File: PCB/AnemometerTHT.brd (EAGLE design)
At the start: 150 x 100 mm, 36 parts, among them IC1 TINY2313A, IC2 74HC151D, IC3 74HC151D, IC4 74HC08D, IC5 LM555N, IC6 74HC138D, IC7 74CH14D, IC8 74HC393D, Q1 16MHz

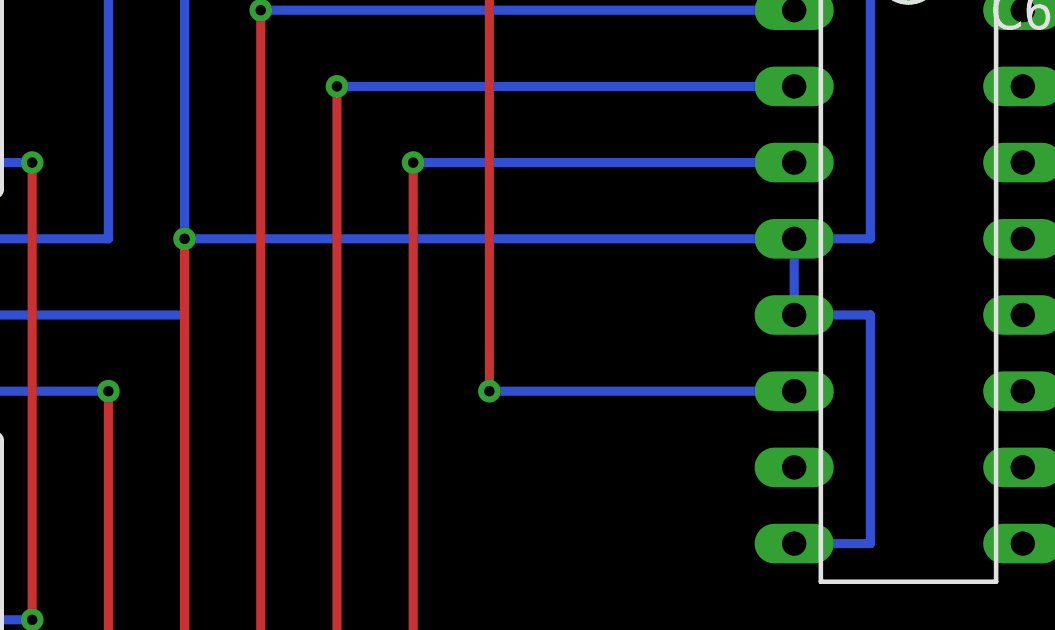
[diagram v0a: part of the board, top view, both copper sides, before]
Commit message: realized that i inverted the wrong signal
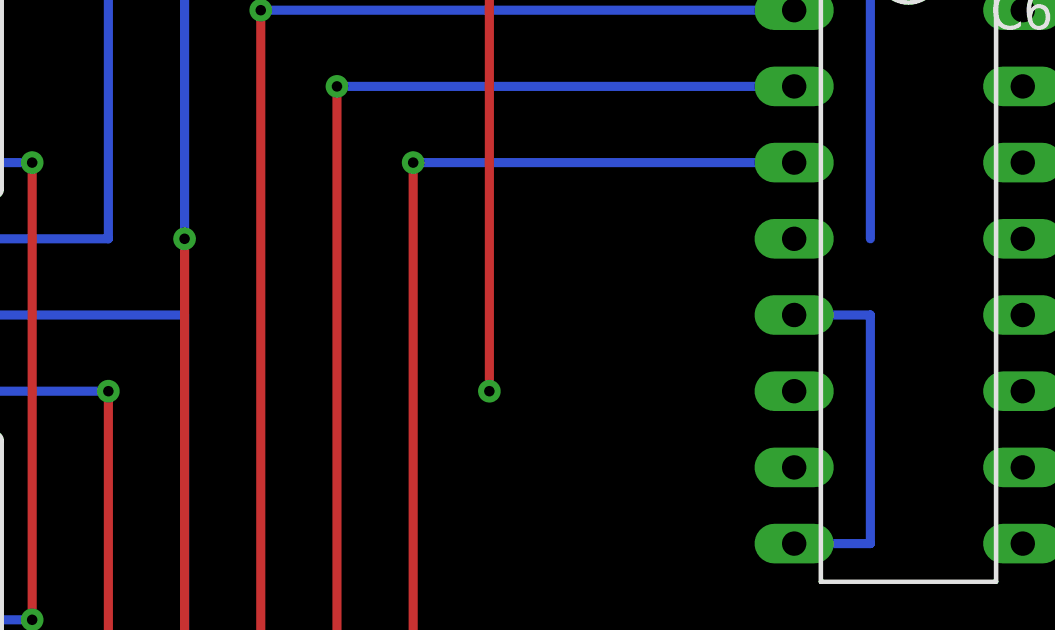
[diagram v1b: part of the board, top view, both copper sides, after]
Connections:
- net GND: no longer IC6.4
- net TRIG: now also IC6.4; no longer IC6.6
- net VCC: now also IC6.6
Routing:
- net GND: track 660.4 -> 635.0 mm
- net TRIG: track 127.0 -> 116.8 mm
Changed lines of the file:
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@@
 <contactref element="IC1" pad="7"/>
 <contactref element="IC8" pad="2"/>
-<contactref element="IC6" pad="6"/>
 <wire x1="30.48" y1="55.88" x2="38.1" y2="55.88" width="0.3048" layer="16"/>
 <wire x1="38.1" y1="55.88" x2="38.1" y2="86.36" width="0.3048" layer="16"/>
@@
 <wire x1="38.1" y1="96.52" x2="58.42" y2="96.52" width="0.3048" layer="16"/>
 <wire x1="58.42" y1="96.52" x2="58.42" y2="91.44" width="0.3048" layer="16"/>
-<wire x1="91.44" y1="76.2" x2="81.28" y2="76.2" width="0.3048" layer="16"/>
 <via x="81.28" y="76.2" extent="1-16" drill="0.35"/>
 <wire x1="81.28" y1="96.52" x2="81.28" y2="76.2" width="0.3048" layer="1"/>
 <via x="81.28" y="96.52" extent="1-16" drill="0.35"/>
 <wire x1="81.28" y1="96.52" x2="58.42" y2="96.52" width="0.3048" layer="16"/>
+<contactref element="IC6" pad="4"/>
+<wire x1="81.28" y1="76.2" x2="91.44" y2="81.28" width="0" layer="19" extent="1-1"/>
 </signal>
 <signal name="UART_TX">
@@
 <contactref element="IC2" pad="12"/>
 <contactref element="IC6" pad="5"/>
-<contactref element="IC6" pad="4"/>
 <contactref element="R8" pad="1"/>
 <contactref element="R3" pad="1"/>
@@
 <via x="132.08" y="81.28" extent="1-16" drill="0.35"/>
 <wire x1="132.08" y1="81.28" x2="132.08" y2="66.04" width="0.3048" layer="1"/>
-<wire x1="91.44" y1="81.28" x2="91.44" y2="78.74" width="0.3048" layer="16"/>
 <wire x1="91.44" y1="71.12" x2="93.98" y2="71.12" width="0.3048" layer="16"/>
 <wire x1="93.98" y1="71.12" x2="93.98" y2="78.74" width="0.3048" layer="16"/>
@@
 <wire x1="83.82" y1="22.86" x2="91.44" y2="22.86" width="0.3048" layer="16"/>
 <wire x1="101.6" y1="22.86" x2="134.62" y2="22.86" width="0.3048" layer="16"/>
-<wire x1="91.44" y1="81.28" x2="71.12" y2="81.28" width="0.3048" layer="16"/>
 <wire x1="134.62" y1="7.62" x2="132.08" y2="7.62" width="0.3048" layer="16"/>
 <via x="132.08" y="7.62" extent="1-16" drill="0.35"/>
@@
 <via x="48.26" y="66.04" extent="1-16" drill="0.35"/>
 <wire x1="48.26" y1="66.04" x2="48.26" y2="68.58" width="0.3048" layer="16"/>
-<wire x1="91.44" y1="81.28" x2="93.98" y2="81.28" width="0.3048" layer="16"/>
 <wire x1="48.26" y1="68.58" x2="48.26" y2="73.66" width="0.3048" layer="16"/>
 <wire x1="48.26" y1="73.66" x2="45.72" y2="73.66" width="0.3048" layer="16"/>
@@
 <wire x1="63.5" y1="45.72" x2="63.5" y2="55.88" width="0.3048" layer="16"/>
 <via x="71.12" y="55.88" extent="1-16" drill="0.35"/>
+<wire x1="91.44" y1="78.74" x2="93.98" y2="81.28" width="0" layer="19" extent="16-16"/>
+<wire x1="83.82" y1="55.88" x2="91.44" y2="71.12" width="0" layer="19" extent="1-1"/>
 </signal>
 <signal name="VCC">
@@
 <wire x1="71.12" y1="43.18" x2="60.96" y2="43.18" width="0.3048" layer="16"/>
 <wire x1="86.36" y1="10.16" x2="58.42" y2="10.16" width="0.3048" layer="16"/>
+<contactref element="IC6" pad="6"/>
+<wire x1="99.06" y1="88.9" x2="91.44" y2="76.2" width="0" layer="19" extent="1-1"/>
 </signal>
 <signal name="PULS">

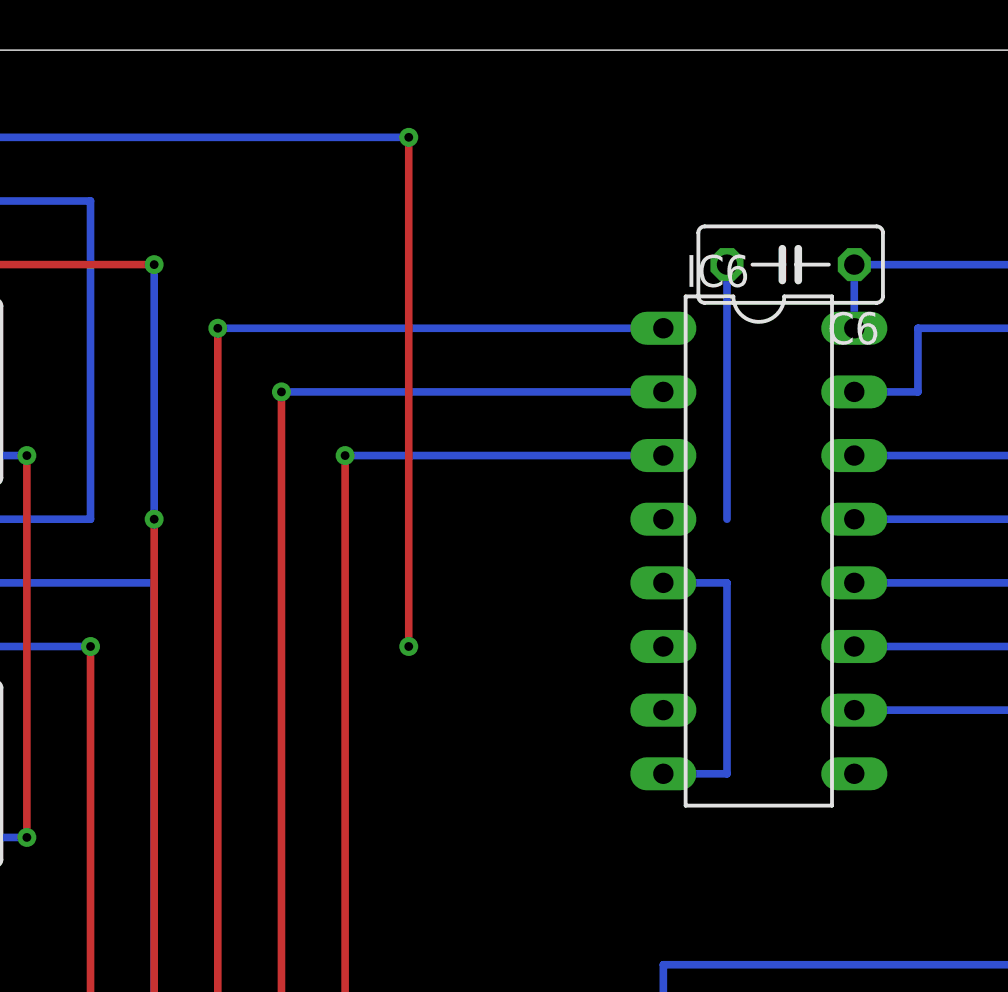
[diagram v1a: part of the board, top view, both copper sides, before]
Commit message: corrected multilexer addressing
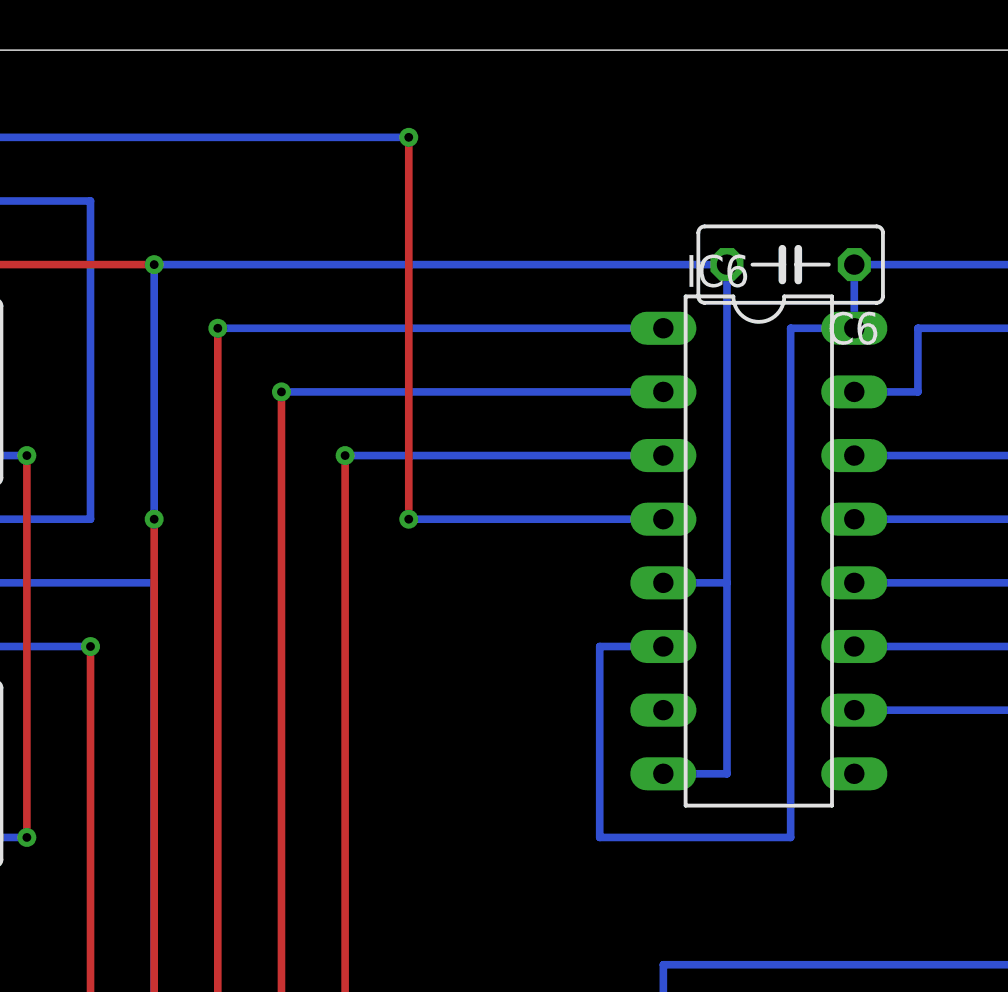
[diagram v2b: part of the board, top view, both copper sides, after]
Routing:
- net VCC: track 563.9 -> 604.5 mm
- net GND: track 635.0 -> 660.4 mm
- net TRIG: track 116.8 -> 121.9 mm
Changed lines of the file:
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@@
 <wire x1="38.1" y1="96.52" x2="58.42" y2="96.52" width="0.3048" layer="16"/>
 <wire x1="58.42" y1="96.52" x2="58.42" y2="91.44" width="0.3048" layer="16"/>
-<via x="81.28" y="76.2" extent="1-16" drill="0.35"/>
-<wire x1="81.28" y1="96.52" x2="81.28" y2="76.2" width="0.3048" layer="1"/>
+<wire x1="81.28" y1="96.52" x2="81.28" y2="81.28" width="0.3048" layer="1"/>
 <via x="81.28" y="96.52" extent="1-16" drill="0.35"/>
 <wire x1="81.28" y1="96.52" x2="58.42" y2="96.52" width="0.3048" layer="16"/>
 <contactref element="IC6" pad="4"/>
-<wire x1="81.28" y1="76.2" x2="91.44" y2="81.28" width="0" layer="19" extent="1-1"/>
+<wire x1="91.44" y1="81.28" x2="81.28" y2="81.28" width="0.3048" layer="16"/>
+<via x="81.28" y="81.28" extent="1-16" drill="0.35"/>
 </signal>
 <signal name="UART_TX">
@@
 <wire x1="93.98" y1="71.12" x2="93.98" y2="78.74" width="0.3048" layer="16"/>
 <wire x1="93.98" y1="78.74" x2="91.44" y2="78.74" width="0.3048" layer="16"/>
-<wire x1="93.98" y1="81.28" x2="93.98" y2="91.44" width="0.3048" layer="16"/>
 <wire x1="83.82" y1="55.88" x2="83.82" y2="53.34" width="0.3048" layer="16"/>
 <wire x1="83.82" y1="53.34" x2="88.9" y2="53.34" width="0.3048" layer="16"/>
@@
 <wire x1="63.5" y1="45.72" x2="63.5" y2="55.88" width="0.3048" layer="16"/>
 <via x="71.12" y="55.88" extent="1-16" drill="0.35"/>
-<wire x1="91.44" y1="78.74" x2="93.98" y2="81.28" width="0" layer="19" extent="16-16"/>
-<wire x1="83.82" y1="55.88" x2="91.44" y2="71.12" width="0" layer="19" extent="1-1"/>
+<wire x1="93.98" y1="91.44" x2="93.98" y2="78.74" width="0.3048" layer="16"/>
+<wire x1="93.98" y1="91.44" x2="71.12" y2="91.44" width="0.3048" layer="16"/>
 </signal>
 <signal name="VCC">
@@
 <wire x1="86.36" y1="10.16" x2="58.42" y2="10.16" width="0.3048" layer="16"/>
 <contactref element="IC6" pad="6"/>
-<wire x1="99.06" y1="88.9" x2="91.44" y2="76.2" width="0" layer="19" extent="1-1"/>
+<wire x1="91.44" y1="76.2" x2="88.9" y2="76.2" width="0.3048" layer="16"/>
+<wire x1="88.9" y1="76.2" x2="88.9" y2="68.58" width="0.3048" layer="16"/>
+<wire x1="88.9" y1="68.58" x2="96.52" y2="68.58" width="0.3048" layer="16"/>
+<wire x1="96.52" y1="68.58" x2="96.52" y2="88.9" width="0.3048" layer="16"/>
+<wire x1="96.52" y1="88.9" x2="99.06" y2="88.9" width="0.3048" layer="16"/>
 </signal>
 <signal name="PULS">

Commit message: added offset corection
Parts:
- added R9: 10k, rcl:0204/7
- added S1, S2: (no value), switch-omron:B3F-10XX
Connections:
- new net SET0: IC1.16, R9.1, S2.1, S2.2
- net GND: now also S1.3, S1.4, S2.3, S2.4
- net RST: now also S1.1, S1.2
- net VCC: now also R9.2
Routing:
- net GND: track 660.4 -> 745.9 mm, vias 19 -> 22
- net SET0: track 0.00 -> 41.5 mm, vias 0 -> 2
- net RST: track 40.6 -> 74.5 mm, vias 0 -> 2
- net VCC: track 604.5 -> 624.8 mm
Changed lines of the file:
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@@
 <attribute name="VALUE" x="104.648" y="16.764" size="1.27" layer="27" ratio="10" rot="R90"/>
+</element>
+<element name="S1" library="switch-omron" library_urn="urn:adsk.eagle:library:377" package="B3F-10XX" package3d_urn="urn:adsk.eagle:package:27496/1" value="" x="15.24" y="12.7" smashed="yes">
+<attribute name="MF" value="" x="15.24" y="12.7" size="1.778" layer="27" display="off"/>
+<attribute name="MPN" value="B3F-1000" x="15.24" y="12.7" size="1.778" layer="27" display="off"/>
+<attribute name="NAME" x="12.192" y="16.383" size="1.27" layer="25" ratio="10"/>
+<attribute name="OC_FARNELL" value="176432" x="15.24" y="12.7" size="1.778" layer="27" display="off"/>
+<attribute name="OC_NEWARK" value="36M3542" x="15.24" y="12.7" size="1.778" layer="27" display="off"/>
+<attribute name="POPULARITY" value="72" x="15.24" y="12.7" size="1.778" layer="27" display="off"/>
+<attribute name="VALUE" x="12.192" y="7.62" size="1.27" layer="27" ratio="10"/>
+</element>
+<element name="S2" library="switch-omron" library_urn="urn:adsk.eagle:library:377" package="B3F-10XX" package3d_urn="urn:adsk.eagle:package:27496/1" value="" x="5.08" y="68.58" smashed="yes" rot="R270">
+<attribute name="MF" value="" x="5.08" y="68.58" size="1.778" layer="27" rot="R270" display="off"/>
+<attribute name="MPN" value="B3F-1000" x="5.08" y="68.58" size="1.778" layer="27" rot="R270" display="off"/>
+<attribute name="NAME" x="8.763" y="71.628" size="1.27" layer="25" ratio="10" rot="R270"/>
+<attribute name="OC_FARNELL" value="176432" x="5.08" y="68.58" size="1.778" layer="27" rot="R270" display="off"/>
+<attribute name="OC_NEWARK" value="36M3542" x="5.08" y="68.58" size="1.778" layer="27" rot="R270" display="off"/>
+<attribute name="POPULARITY" value="72" x="5.08" y="68.58" size="1.778" layer="27" rot="R270" display="off"/>
+<attribute name="VALUE" x="0" y="71.628" size="1.27" layer="27" ratio="10" rot="R270"/>
+</element>
+<element name="R9" library="rcl" library_urn="urn:adsk.eagle:library:334" package="0204/7" package3d_urn="urn:adsk.eagle:package:23498/2" value="10k" x="10.16" y="41.91" smashed="yes" rot="R270">
+<attribute name="NAME" x="11.4554" y="44.45" size="0.9906" layer="25" ratio="10" rot="R270"/>
+<attribute name="POPULARITY" value="79" x="10.16" y="41.91" size="1.778" layer="27" rot="R270" display="off"/>
+<attribute name="SPICEPREFIX" value="R" x="10.16" y="41.91" size="1.778" layer="27" rot="R270" display="off"/>
+<attribute name="VALUE" x="9.6774" y="43.5356" size="0.9906" layer="27" ratio="10" rot="R270"/>
 </element>
 </elements>
@@
 <wire x1="33.02" y1="22.86" x2="33.02" y2="40.64" width="0.3048" layer="16"/>
 <wire x1="33.02" y1="40.64" x2="30.48" y2="40.64" width="0.3048" layer="16"/>
+<contactref element="S1" pad="2"/>
+<contactref element="S1" pad="1"/>
+<wire x1="18.4912" y1="14.9606" x2="11.9888" y2="14.9606" width="0.3048" layer="16"/>
+<wire x1="11.9888" y1="14.9606" x2="10.4394" y2="14.9606" width="0.3048" layer="16"/>
+<wire x1="10.4394" y1="14.9606" x2="10.16" y2="15.24" width="0.3048" layer="16"/>
+<via x="10.16" y="15.24" extent="1-16" drill="0.35"/>
+<wire x1="10.16" y1="15.24" x2="10.16" y2="30.48" width="0.3048" layer="1"/>
+<wire x1="10.16" y1="30.48" x2="17.78" y2="30.48" width="0.3048" layer="1"/>
+<via x="17.78" y="30.48" extent="1-16" drill="0.35"/>
+<wire x1="17.78" y1="30.48" x2="17.78" y2="27.94" width="0.3048" layer="16"/>
 </signal>
 <signal name="MOSI">
@@
 <wire x1="93.98" y1="91.44" x2="93.98" y2="78.74" width="0.3048" layer="16"/>
 <wire x1="93.98" y1="91.44" x2="71.12" y2="91.44" width="0.3048" layer="16"/>
+<contactref element="S1" pad="3"/>
+<contactref element="S1" pad="4"/>
+<wire x1="18.4912" y1="10.4394" x2="11.9888" y2="10.4394" width="0.3048" layer="16"/>
+<wire x1="11.9888" y1="10.4394" x2="11.7094" y2="10.16" width="0.3048" layer="16"/>
+<wire x1="11.7094" y1="10.16" x2="10.16" y2="10.16" width="0.3048" layer="16"/>
+<via x="10.16" y="10.16" extent="1-16" drill="0.35"/>
+<wire x1="10.16" y1="10.16" x2="7.62" y2="10.16" width="0.3048" layer="1"/>
+<wire x1="7.62" y1="10.16" x2="7.62" y2="33.02" width="0.3048" layer="1"/>
+<wire x1="7.62" y1="33.02" x2="15.24" y2="33.02" width="0.3048" layer="1"/>
+<via x="15.24" y="33.02" extent="1-16" drill="0.35"/>
+<contactref element="S2" pad="4"/>
+<contactref element="S2" pad="3"/>
+<wire x1="2.8194" y1="71.8312" x2="2.8194" y2="65.3288" width="0.3048" layer="16"/>
+<wire x1="2.8194" y1="71.8312" x2="2.54" y2="72.1106" width="0.3048" layer="16"/>
+<wire x1="2.54" y1="72.1106" x2="2.54" y2="73.66" width="0.3048" layer="16"/>
+<via x="2.54" y="73.66" extent="1-16" drill="0.35"/>
+<wire x1="2.54" y1="73.66" x2="30.48" y2="73.66" width="0.3048" layer="1"/>
+<wire x1="30.48" y1="73.66" x2="30.48" y2="66.04" width="0.3048" layer="1"/>
 </signal>
 <signal name="VCC">
@@
 <wire x1="96.52" y1="68.58" x2="96.52" y2="88.9" width="0.3048" layer="16"/>
 <wire x1="96.52" y1="88.9" x2="99.06" y2="88.9" width="0.3048" layer="16"/>
+<contactref element="R9" pad="2"/>
+<wire x1="10.16" y1="38.1" x2="10.16" y2="22.86" width="0.3048" layer="16"/>
+<wire x1="10.16" y1="22.86" x2="15.24" y2="22.86" width="0.3048" layer="16"/>
 </signal>
 <signal name="PULS">
@@
 <wire x1="93.98" y1="43.18" x2="93.98" y2="48.26" width="0.3048" layer="16"/>
 </signal>
+<signal name="SET0">
+<contactref element="IC1" pad="16"/>
+<contactref element="S2" pad="2"/>
+<contactref element="S2" pad="1"/>
+<wire x1="7.3406" y1="71.8312" x2="7.3406" y2="65.3288" width="0.3048" layer="16"/>
+<wire x1="7.3406" y1="65.3288" x2="7.62" y2="65.0494" width="0.3048" layer="16"/>
+<wire x1="7.62" y1="65.0494" x2="7.62" y2="63.5" width="0.3048" layer="16"/>
+<via x="7.62" y="63.5" extent="1-16" drill="0.35"/>
+<wire x1="7.62" y1="63.5" x2="7.62" y2="50.8" width="0.3048" layer="1"/>
+<wire x1="7.62" y1="50.8" x2="10.16" y2="50.8" width="0.3048" layer="1"/>
+<via x="10.16" y="50.8" extent="1-16" drill="0.35"/>
+<wire x1="10.16" y1="50.8" x2="22.86" y2="50.8" width="0.3048" layer="16"/>
+<contactref element="R9" pad="1"/>
+<wire x1="10.16" y1="45.72" x2="10.16" y2="50.8" width="0.3048" layer="16"/>
+</signal>
 </signals>
